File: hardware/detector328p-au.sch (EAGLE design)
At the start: 61 parts, among them J1 AVR_SPI_PRG_6NS, K1 SRD-05VDC-SL-C, Q1 BS170, Q2 16MHz, T1 BC337, T2 BC337, T3 BC337, U1 ATMEGA328P-AU

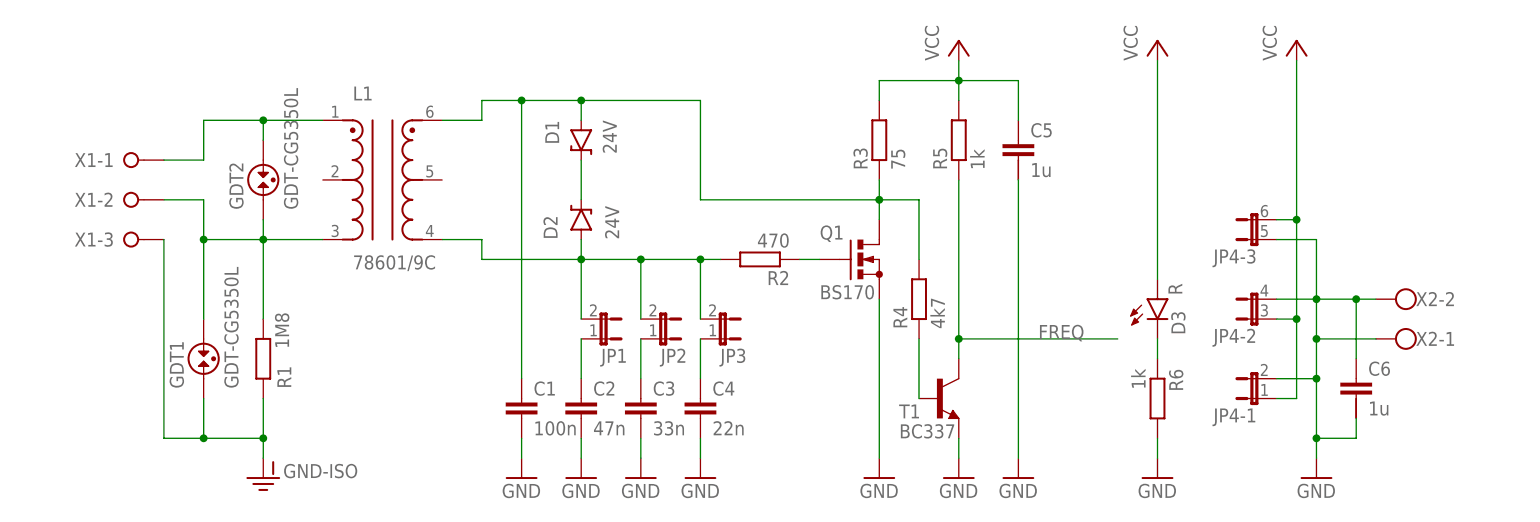
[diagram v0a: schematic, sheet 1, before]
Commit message: hardware-m328p-au: preparing schematics for board creation
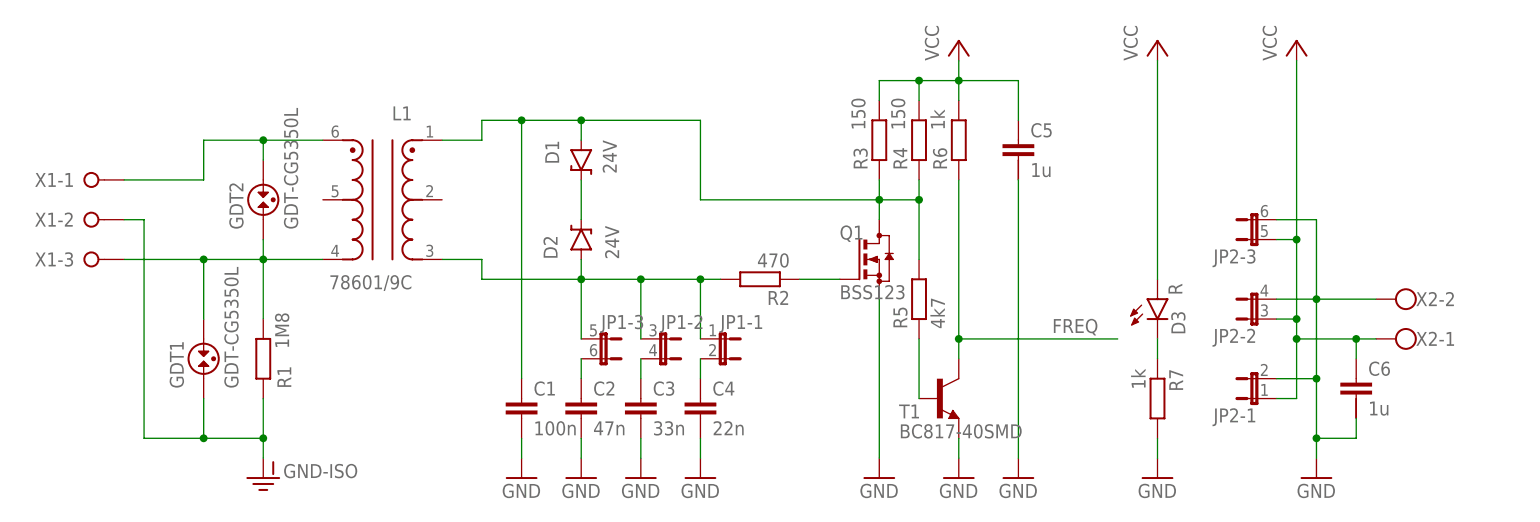
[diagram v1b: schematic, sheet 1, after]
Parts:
- removed JP5: (no value), jumper:JP2E
- removed JP6: (no value), jumper:JP4E
- added PB1, PB2: TACTILE-SWITCH-PTH, GeekAmmo:TACTILE-SWITCH-PTH
- added R20, R21: 1k, resistor:R-EU_R0603
- C7, C8: device resistor:C-EU050-024X044 -> resistor:C-EUC0603
- D10, D12, D3, D4, D6, D8, D9: device SparkFun-LED:LED3MM -> SparkFun-LED:LED0603
- D11: value G -> Y; device SparkFun-LED:LED3MM -> SparkFun-LED:LED0603
- D13: value 1N4148DO35-7 -> G; device diode:1N4148DO35-7 -> SparkFun-LED:LED0603
- D5: value R -> 1N4148DO35-7; device SparkFun-LED:LED3MM -> diode:1N4148DO35-7
- D7: value Y -> R; device SparkFun-LED:LED3MM -> SparkFun-LED:LED0603
- JP1, JP2: device SparkFun-Retired:JUMPER-2PTH -> jumper:JP3QE
- JP3: device SparkFun-Retired:JUMPER-2PTH -> jumper:JP2E
- JP4: device jumper:JP3QE -> jumper:JP4E
- Q1: value BS170 -> BSS123; device transistor-small-signal:BS170 -> transistor-small-signal:BSS123
- R1, R12, R13, R15, R17, R2, R6, R7: device resistor:R-EU_0204/5 -> resistor:R-EU_R0603
- R10, R16, R9: value 1k -> 4k7; device resistor:R-EU_0204/5 -> resistor:R-EU_R0603
- R11: value 10k -> 1k; device resistor:R-EU_0204/5 -> resistor:R-EU_R0603
- R14: value 1k -> 10k; device resistor:R-EU_0204/5 -> resistor:R-EU_R0603
- R18, R19, R8: value 4k7 -> 1k; device resistor:R-EU_0204/5 -> resistor:R-EU_R0603
- R3: value 75 -> 150; device resistor:R-EU_0204/7 -> resistor:R-EU_R0603
- R4: value 4k7 -> 150; device resistor:R-EU_0204/5 -> resistor:R-EU_R0603
- R5: value 1k -> 4k7
- T1: value BC337 -> BC817-40SMD; device transistor:BC337-NPN-TO92-CBE -> transistor-npn:BC817-40SMD
- T2, T3: value BC337 -> BC817; device transistor:BC337-NPN-TO92-CBE -> transistor-npn:BC817-40SMD
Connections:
- removed net N$34 (its old number): D6.A, R10.2
- removed net N$38: R19.2, R8.1, U1.PB0
- new net N$27: D8.A, R15.2
- new net N$46: R13.1, U1.PB0
- new net N$47: PB1.1, R10.1, R13.2, R9.2
- net FREQ: now also R16.1, R6.1; no longer R18.1, R5.1
- net GND: now also D13.C, JP2-1.2, JP2-2.2, JP2-3.2, JP3.3, JP4.1, PB2.3, R7.2; no longer C6.1, D5.C, JP4-1.2, JP4-2.2, JP4-3.1, JP5.3, JP6.1, R6.2, X2-1.KL
- net GND-ISO: now also X1-2.KL; no longer X1-3.KL
- net N$11: now also JP1-3.2; no longer JP1.1
- net N$14: now also L1.1, R4.1, R5.2; no longer L1.6, R4.2
- net N$16: now also D9.A, R17.2; no longer D8.A, R13.2
- net N$17: now also D10.A, R18.2; no longer D9.A, R14.2
- net N$18: now also D11.A, R19.2; no longer D10.A, R15.2
- net N$19: now also D12.A, R20.2; no longer D11.A, R16.2
- net N$2: now also R5.1; no longer R4.1
- net N$20: now also R10.2; no longer R8.2
- net N$21: now also L1.4, X1-3.KL; no longer L1.3, X1-2.KL
- net N$22: now also R7.1; no longer R6.1
- net N$23: now also JP3.2; no longer JP5.2
- net N$24: now also R8.1; no longer R7.1
- net N$25: now also R17.1; no longer R13.1
- net N$26: now also R15.1; no longer R12.1
- net N$28: now also R18.1; no longer R14.1
- net N$29: now also R19.1; no longer R15.1
- net N$30: now also PB2.1, R14.1; no longer R11.1
- net N$31: now also R20.1; no longer R16.1
- net N$32: now also D13.A, R21.2; no longer D12.A, R17.2
- net N$33: now also R21.1; no longer R17.1
- net N$35: now also D6.A, R11.2; no longer D5.A, R9.2
- net N$36: now also R12.1; no longer R10.1
- net N$37: now also R11.1; no longer R9.1
- net N$39: now also D5.A; no longer D13.A
- net N$4: now also JP1-2.2; no longer JP2.1
- net N$40: now also R9.1; no longer R19.1
- net N$44: now also JP4.4; no longer JP6.4
- net N$45: now also JP4.3; no longer JP6.3
- net N$5: now also JP1-1.2; no longer JP3.1
- net N$6: now also JP1-1.1, JP1-2.1, JP1-3.1, L1.3; no longer JP1.2, JP2.2, JP3.2, L1.4
- net N$7: now also L1.6; no longer L1.1
- net N$9: now also R16.2; no longer R18.2
- net VCC: now also C6.1, D5.C, JP2-1.1, JP2-2.1, JP2-3.1, JP3.1, JP4.2, PB1.3, R14.2, R4.2, R6.2, R8.2, X2-1.KL; no longer D13.C, JP4-1.1, JP4-2.1, JP4-3.2, JP5.1, JP6.2, R11.2, R5.2, R7.2
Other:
- moved on the sheet: D1, D10, D11, D12, D2, D6, D7, D8, D9, GDT2, L1, R10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

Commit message: hardware-m328p-au: MCU referred from gate433.lbr
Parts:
- U1: device Atmel_By_element14_Batch_1-00:ATMEGA328P-AU -> detector:ATMEGA328P-AU
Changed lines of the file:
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@@
 <grid distance="0.1" unitdist="inch" unit="inch" style="lines" multiple="1" display="no" altdistance="0.01" altunitdist="inch" altunit="inch"/>
 <layers>
-<layer number="1" name="Top" color="4" fill="1" visible="yes" active="no"/>
-<layer number="2" name="Route2" color="1" fill="3" visible="yes" active="no"/>
-<layer number="3" name="Route3" color="4" fill="3" visible="yes" active="no"/>
-<layer number="4" name="Route4" color="1" fill="4" visible="yes" active="no"/>
-<layer number="5" name="Route5" color="4" fill="4" visible="yes" active="no"/>
-<layer number="6" name="Route6" color="1" fill="8" visible="yes" active="no"/>
-<layer number="7" name="Route7" color="4" fill="8" visible="yes" active="no"/>
-<layer number="8" name="Route8" color="1" fill="2" visible="yes" active="no"/>
-<layer number="9" name="Route9" color="4" fill="2" visible="yes" active="no"/>
-<layer number="10" name="Route10" color="1" fill="7" visible="yes" active="no"/>
-<layer number="11" name="Route11" color="4" fill="7" visible="yes" active="no"/>
-<layer number="12" name="Route12" color="1" fill="5" visible="yes" active="no"/>
-<layer number="13" name="Route13" color="4" fill="5" visible="yes" active="no"/>
-<layer number="14" name="Route14" color="1" fill="6" visible="yes" active="no"/>
-<layer number="15" name="Route15" color="4" fill="6" visible="yes" active="no"/>
-<layer number="16" name="Bottom" color="1" fill="1" visible="yes" active="no"/>
-<layer number="17" name="Pads" color="2" fill="1" visible="yes" active="no"/>
-<layer number="18" name="Vias" color="2" fill="1" visible="yes" active="no"/>
-<layer number="19" name="Unrouted" color="6" fill="1" visible="yes" active="no"/>
-<layer number="20" name="Dimension" color="15" fill="1" visible="yes" active="no"/>
-<layer number="21" name="tPlace" color="7" fill="1" visible="yes" active="no"/>
-<layer number="22" name="bPlace" color="7" fill="1" visible="yes" active="no"/>
-<layer number="23" name="tOrigins" color="15" fill="1" visible="yes" active="no"/>
-<layer number="24" name="bOrigins" color="15" fill="1" visible="yes" active="no"/>
-<layer number="25" name="tNames" color="7" fill="1" visible="yes" active="no"/>
-<layer number="26" name="bNames" color="7" fill="1" visible="yes" active="no"/>
-<layer number="27" name="tValues" color="7" fill="1" visible="yes" active="no"/>
-<layer number="28" name="bValues" color="7" fill="1" visible="yes" active="no"/>
+<layer number="1" name="Top" color="4" fill="1" visible="no" active="no"/>
+<layer number="2" name="Route2" color="1" fill="3" visible="no" active="no"/>
+<layer number="3" name="Route3" color="4" fill="3" visible="no" active="no"/>
+<layer number="4" name="Route4" color="1" fill="4" visible="no" active="no"/>
+<layer number="5" name="Route5" color="4" fill="4" visible="no" active="no"/>
+<layer number="6" name="Route6" color="1" fill="8" visible="no" active="no"/>
+<layer number="7" name="Route7" color="4" fill="8" visible="no" active="no"/>
+<layer number="8" name="Route8" color="1" fill="2" visible="no" active="no"/>
+<layer number="9" name="Route9" color="4" fill="2" visible="no" active="no"/>
+<layer number="10" name="Route10" color="1" fill="7" visible="no" active="no"/>
+<layer number="11" name="Route11" color="4" fill="7" visible="no" active="no"/>
+<layer number="12" name="Route12" color="1" fill="5" visible="no" active="no"/>
+<layer number="13" name="Route13" color="4" fill="5" visible="no" active="no"/>
+<layer number="14" name="Route14" color="1" fill="6" visible="no" active="no"/>
+<layer number="15" name="Route15" color="4" fill="6" visible="no" active="no"/>
+<layer number="16" name="Bottom" color="1" fill="1" visible="no" active="no"/>
+<layer number="17" name="Pads" color="2" fill="1" visible="no" active="no"/>
+<layer number="18" name="Vias" color="2" fill="1" visible="no" active="no"/>
+<layer number="19" name="Unrouted" color="6" fill="1" visible="no" active="no"/>
+<layer number="20" name="Dimension" color="15" fill="1" visible="no" active="no"/>
+<layer number="21" name="tPlace" color="7" fill="1" visible="no" active="no"/>
+<layer number="22" name="bPlace" color="7" fill="1" visible="no" active="no"/>
+<layer number="23" name="tOrigins" color="15" fill="1" visible="no" active="no"/>
+<layer number="24" name="bOrigins" color="15" fill="1" visible="no" active="no"/>
+<layer number="25" name="tNames" color="7" fill="1" visible="no" active="no"/>
+<layer number="26" name="bNames" color="7" fill="1" visible="no" active="no"/>
+<layer number="27" name="tValues" color="7" fill="1" visible="no" active="no"/>
+<layer number="28" name="bValues" color="7" fill="1" visible="no" active="no"/>
 <layer number="29" name="tStop" color="7" fill="3" visible="no" active="no"/>
 <layer number="30" name="bStop" color="7" fill="6" visible="no" active="no"/>
@@
 <layer number="35" name="tGlue" color="7" fill="4" visible="no" active="no"/>
 <layer number="36" name="bGlue" color="7" fill="5" visible="no" active="no"/>
-<layer number="37" name="tTest" color="7" fill="1" visible="yes" active="no"/>
-<layer number="38" name="bTest" color="7" fill="1" visible="yes" active="no"/>
+<layer number="37" name="tTest" color="7" fill="1" visible="no" active="no"/>
+<layer number="38" name="bTest" color="7" fill="1" visible="no" active="no"/>
 <layer number="39" name="tKeepout" color="4" fill="11" visible="no" active="no"/>
 <layer number="40" name="bKeepout" color="1" fill="11" visible="no" active="no"/>
@@
 <layer number="44" name="Drills" color="7" fill="1" visible="no" active="no"/>
 <layer number="45" name="Holes" color="7" fill="1" visible="no" active="no"/>
-<layer number="46" name="Milling" color="3" fill="1" visible="yes" active="no"/>
-<layer number="47" name="Measures" color="7" fill="1" visible="yes" active="no"/>
-<layer number="48" name="Document" color="7" fill="1" visible="yes" active="no"/>
-<layer number="49" name="Reference" color="7" fill="1" visible="yes" active="no"/>
-<layer number="50" name="dxf" color="7" fill="1" visible="yes" active="no"/>
-<layer number="51" name="tDocu" color="7" fill="1" visible="yes" active="no"/>
-<layer number="52" name="bDocu" color="7" fill="1" visible="yes" active="no"/>
-<layer number="53" name="tGND_GNDA" color="7" fill="9" visible="yes" active="no"/>
-<layer number="54" name="bGND_GNDA" color="1" fill="9" visible="yes" active="no"/>
-<layer number="56" name="wert" color="7" fill="1" visible="yes" active="no"/>
-<layer number="57" name="tCAD" color="7" fill="1" visible="yes" active="no"/>
-<layer number="59" name="tCarbon" color="7" fill="1" visible="yes" active="no"/>
-<layer number="60" name="bCarbon" color="7" fill="1" visible="yes" active="no"/>
+<layer number="46" name="Milling" color="3" fill="1" visible="no" active="no"/>
+<layer number="47" name="Measures" color="7" fill="1" visible="no" active="no"/>
+<layer number="48" name="Document" color="7" fill="1" visible="no" active="no"/>
+<layer number="49" name="Reference" color="7" fill="1" visible="no" active="no"/>
+<layer number="50" name="dxf" color="7" fill="1" visible="no" active="no"/>
+<layer number="51" name="tDocu" color="7" fill="1" visible="no" active="no"/>
+<layer number="52" name="bDocu" color="7" fill="1" visible="no" active="no"/>
+<layer number="53" name="tGND_GNDA" color="7" fill="9" visible="no" active="no"/>
+<layer number="54" name="bGND_GNDA" color="1" fill="9" visible="no" active="no"/>
+<layer number="56" name="wert" color="7" fill="1" visible="no" active="no"/>
+<layer number="57" name="tCAD" color="7" fill="1" visible="no" active="no"/>
+<layer number="59" name="tCarbon" color="7" fill="1" visible="no" active="no"/>
+<layer number="60" name="bCarbon" color="7" fill="1" visible="no" active="no"/>
 <layer number="90" name="Modules" color="5" fill="1" visible="yes" active="yes"/>
 <layer number="91" name="Nets" color="2" fill="1" visible="yes" active="yes"/>
@@
 <part name="GND18" library="supply1" deviceset="GND" device=""/>
 <part name="R14" library="resistor" deviceset="R-EU_" device="R0603" value="10k"/>
-<part name="U1" library="Atmel_By_element14_Batch_1-00" deviceset="ATMEGA328P-AU" device=""/>
+<part name="U1" library="detector" deviceset="ATMEGA328P-AU" device=""/>
 <part name="R16" library="resistor" deviceset="R-EU_" device="R0603" value="4k7"/>
 <part name="GND16" library="supply1" deviceset="GND" device=""/>
